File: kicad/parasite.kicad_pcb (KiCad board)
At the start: 2 copper layers, 22 x 126.4 mm, 31 parts, among them Q1 MMBT3906, Q4 Q_Photo_NPN, SW1 B3U-1000P, U1 E73-2G4M08S1C, U2 SHTC3, Y1 32.768kHz

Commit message: updated PCB with 3 zones and soil temp sensor
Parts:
- removed TP5: CPARA, TestPoint:TestPoint_Pad_D1.0mm
- removed TP6: PWM, TestPoint:TestPoint_Pad_D1.0mm
- added C5: 1n, Capacitor_SMD:C_0402_1005Metric, F.Cu at (59.9, 55.9)
- added C6: 1n, Capacitor_SMD:C_0402_1005Metric, F.Cu at (66.3, 55.9)
- added C7: 100n, Capacitor_SMD:C_0402_1005Metric, F.Cu at (71.0, 326.2)
- added D3: LL4148, Diode_SMD:D_MiniMELF, F.Cu at (59.5, 59.7)
- added D4: LL4148, Diode_SMD:D_MiniMELF, F.Cu at (65.6, 59.7)
- added Q2: MMBT3906, Package_TO_SOT_SMD:SOT-23, F.Cu at (62.5, 59.0)
- added Q3: MMBT3906, Package_TO_SOT_SMD:SOT-23, F.Cu at (68.6, 59.0)
- added R11: 10k, Resistor_SMD:R_0402_1005Metric, F.Cu at (67.7, 56.0)
- added R12: 10k, Resistor_SMD:R_0402_1005Metric, F.Cu at (69.6, 55.9)
- added R13: 1M, Resistor_SMD:R_0402_1005Metric, F.Cu at (64.9, 55.9)
- added R3: 10k, Resistor_SMD:R_0402_1005Metric, F.Cu at (61.7, 55.9)
- added R5: 10k, Resistor_SMD:R_0402_1005Metric, F.Cu at (63.5, 55.9)
- added R9: 1M, Resistor_SMD:R_0402_1005Metric, F.Cu at (58.8, 55.9)
- added U3: TMP117xxDRV, Package_SON:WSON-6-1EP_2x2mm_P0.65mm_EP1x1.6mm, F.Cu at (68.0, 325.9)
- moved R4 16.2 mm to (76.3, 64.5), turned to 0 degrees
- moved R1 15.4 mm to (76.3, 59.9), turned to 180 degrees
- moved Q1 11.2 mm to (75.5, 62.2), turned to -90 degrees
- moved D1 9.57 mm to (72.5, 63.2), turned to -90 degrees
- moved C2 4.71 mm to (74.6, 57.8), turned to 180 degrees
- moved C1 3.37 mm to (73.1, 59.4), turned to 90 degrees
- moved R6 0.42 mm to (71.8, 59.4), turned to 90 degrees
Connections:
- net CPARA renamed CPARA_1
- net SENS_OUT renamed SENS_OUT_1
- U1 pad 18: unconnected-(U1B-P0.04/AIN2-Pad18) -> SENS_OUT_3
- U1 pad 9: unconnected-(U1B-P0.31/AIN7-Pad9) -> SENS_OUT_2
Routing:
- net SDA: track 24.5 -> 309.7 mm
- net SCL: track 22.2 -> 302.8 mm
- net +3V0: track 76.5 -> 344.0 mm, vias 8 -> 11
- net CPARA_2: track 0.00 -> 265.0 mm
- net CPARA_3: track 0.00 -> 186.6 mm
- net PWM: track 20.1 -> 68.4 mm
- net SENS_OUT_3: track 0.00 -> 31.7 mm, vias 0 -> 2
- net SENS_OUT_2: track 0.00 -> 20.9 mm
- net GND: track 22.2 -> 37.6 mm, vias 29 -> 73
- net CPARA_1: track 95.6 -> 102.5 mm
- net SENS_OUT_1: track 38.5 -> 43.6 mm
- net Net-(Q3-B): track 0.00 -> 1.60 mm
- net Net-(Q2-B): track 0.00 -> 1.60 mm
- net BTN1: track 7.22 -> 8.63 mm
- net Net-(Q1-B): track 5.30 -> 3.92 mm
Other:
- board size 22 x 126.4 mm -> 22 x 309.8 mm
- rule pad_to_mask_clearance: 0.051 -> 0
- board text added: "b-parasite-long 0.0.1 rbaron.net acamilo.github.io"
- board text removed: "b-parasite 2.0.0 rbaron.net"

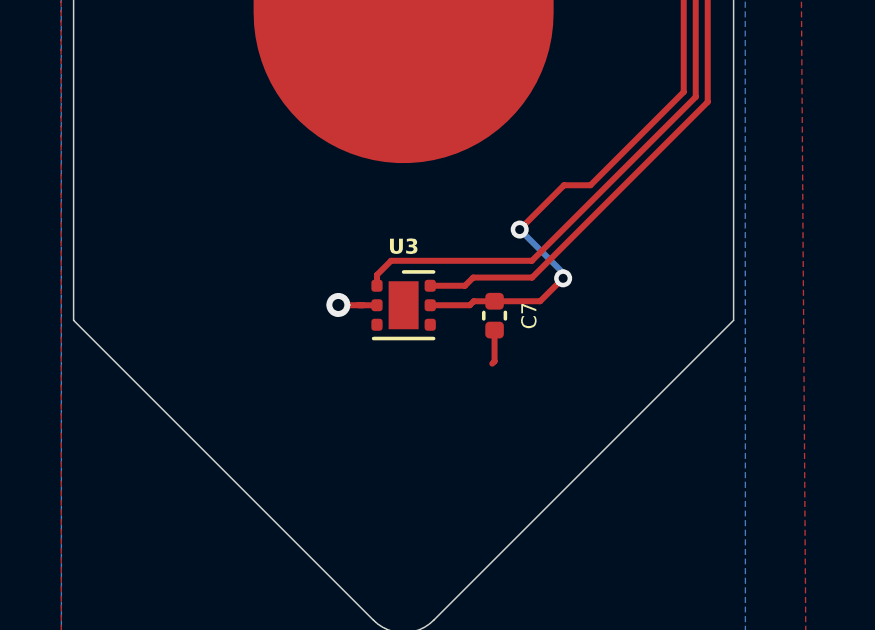
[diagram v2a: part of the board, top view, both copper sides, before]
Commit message: Fixed i2c address pin issue
Connected pin to 3v to program 0x49 address
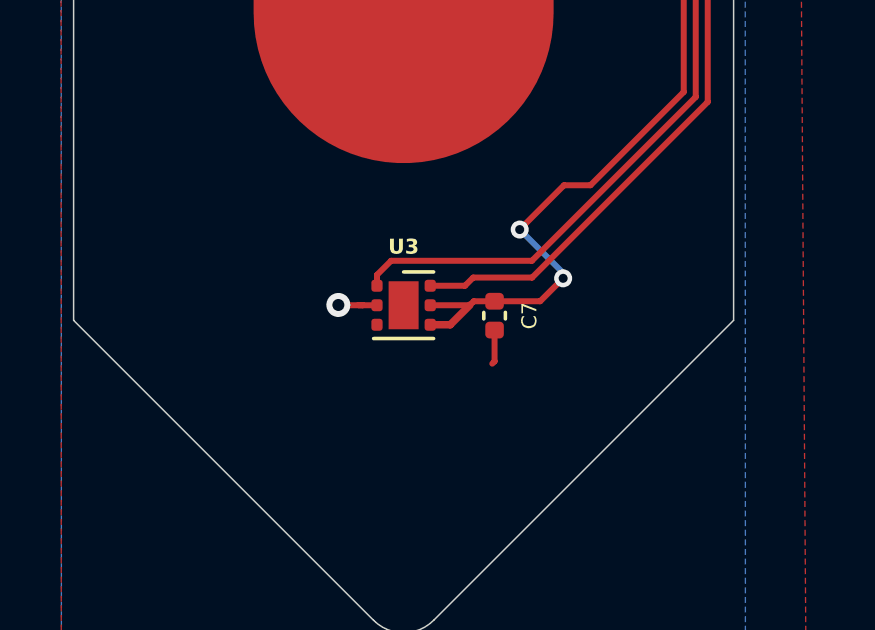
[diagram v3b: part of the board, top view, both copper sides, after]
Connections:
- U3 pad 4: unconnected-(U3-ADD0-Pad4) -> +3V0
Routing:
- net +3V0: track 344.0 -> 345.6 mm
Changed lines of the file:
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@@
   (net 49 "Net-(Q3-B)")
   (net 50 "unconnected-(U3-ALERT-Pad3)")
-  (net 51 "unconnected-(U3-ADD0-Pad4)")
   (footprint "Capacitor_SMD:C_0402_1005Metric" (layer "F.Cu")
     (at 73.1148 59.3738 90)
@@
     (descr "WSON, 6 Pin (http://www.ti.com/lit/ds/symlink/tps61040.pdf#page=35), generated with kicad-footprint-generator ipc_noLead_generator.py")
     (tags "WSON NoLead")
+    (property "LCSC" "C2803242")
     (property "Sheetfile" "parasite.kicad_sch")
     (property "Sheetname" "")
@@
       (net 50 "unconnected-(U3-ALERT-Pad3)") (pinfunction "ALERT") (pintype "open_collector"))
     (pad "4" smd roundrect (at 0.8875 0.65) (size 0.375 0.4) (layers "F.Cu" "F.Paste" "F.Mask") (roundrect_rratio 0.25)
-      (net 51 "unconnected-(U3-ADD0-Pad4)") (pinfunction "ADD0") (pintype "input"))
+      (net 6 "+3V0") (pinfunction "ADD0") (pintype "input"))
     (pad "5" smd roundrect (at 0.8875 0) (size 0.375 0.4) (layers "F.Cu" "F.Paste" "F.Mask") (roundrect_rratio 0.25)
       (net 6 "+3V0") (pinfunction "V+") (pintype "power_in"))
@@
   (segment (start 72.5534 325.7438) (end 73.318 324.9792) (width 0.2) (layer "F.Cu") (net 6))
   (segment (start 75.20752 52.88448) (end 75.20752 50.97948) (width 0.2) (layer "F.Cu") (net 6))
+  (segment (start 68.8875 326.5268) (end 69.555 326.5268) (width 0.25) (layer "F.Cu") (net 6))
   (segment (start 76.3406 57.822) (end 76.62 57.5426) (width 0.5) (layer "F.Cu") (net 6))
   (segment (start 76.366 33.184) (end 77.382 32.168) (width 0.5) (layer "F.Cu") (net 6))
@@
   (segment (start 70.048489 44.273039) (end 67.707511 44.273039) (width 0.2) (layer "F.Cu") (net 6))
   (segment (start 77.3376 318.768314) (end 74.228957 321.876957) (width 0.2) (layer "F.Cu") (net 6))
+  (segment (start 69.555 326.5268) (end 70.205 325.8768) (width 0.25) (layer "F.Cu") (net 6))
   (segment (start 75.20752 50.97948) (end 75.858 50.329) (width 0.2) (layer "F.Cu") (net 6))
   (segment (start 76.6962 65.3404) (end 77.3376 65.9818) (width 0.2) (layer "F.Cu") (net 6))
